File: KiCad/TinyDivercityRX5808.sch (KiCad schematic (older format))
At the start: 18 parts

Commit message: Prototype board is ready
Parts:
- removed J?: RXA, symbol Conn_01x08
- removed J?: RXB, symbol Conn_01x08
- removed J?: Video, symbol Conn_01x02
- removed J?: Googles, symbol Conn_01x05
- removed SW?: SW_Push, symbol SW_Push
- added D2: LED, LEDs:LED_0603, symbol LED
- added J1: Googles, Pin_Headers:Pin_Header_Angled_1x09_Pitch2.54mm, symbol Conn_01x09
- added J2: RX_A, Pin_Headers:Pin_Header_Straight_1x09_Pitch2.54mm, symbol Conn_01x09
- added J3: RX_B, Pin_Headers:Pin_Header_Straight_1x09_Pitch2.54mm, symbol Conn_01x09
- added J4: PROG, Pin_Headers:Pin_Header_Straight_2x05_Pitch2.54mm, symbol Conn_02x05_Odd_Even
- added JP1: Jumper, Pin_Headers:Pin_Header_Straight_1x02_Pitch2.54mm, symbol Jumper
- added R7: 30, Resistors_SMD:R_0603, symbol R
- added R8: 1K, Resistors_SMD:R_0603, symbol R
- added R9: 10K, Resistors_SMD:R_0603, symbol R
- added SW1: SW_DPST, Buttons_Switches_THT:SW_PUSH_6mm_h7.3mm, symbol SW_DPST
- R6: renamed from R?; value 300 -> 1K
- gave numbers to parts that had none: 12
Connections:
- net labels added: AUD_IN, AUD_OUT, MISO, MOSI, RST
- wire segments 67 -> 82
- no-connect marks 0 -> 5
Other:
- moved on the sheet: D1, R4, R5, R6

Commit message: Modified test board
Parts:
- added JP2: JVB, Pin_Headers:Pin_Header_Straight_1x02_Pitch2.54mm, symbol Jumper
- added JP3: JWA, Pin_Headers:Pin_Header_Straight_1x02_Pitch2.54mm, symbol Jumper
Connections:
- net VideoA: now also JP3.1; no longer U1.4 (NC)
- net VideoB: now also JP2.1; no longer U1.6 (NO)
- new net: JP3.2, U1.4 (NC)
- new net: JP2.2, U1.6 (NO)
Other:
- moved on the sheet: JP1
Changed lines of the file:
@@
 $EndComp
 $Comp
-L GND #PWR12
+L GND #PWR11
 U 1 1 5A0C59D1
 P 7000 3700
-F 0 "#PWR12" H 7000 3450 50  0001 C CNN
+F 0 "#PWR11" H 7000 3450 50  0001 C CNN
 F 1 "GND" H 7000 3550 50  0000 C CNN
 F 2 "" H 7000 3700 50  0001 C CNN
@@
 	1    0    0    -1
 $EndComp
-Text Label 6350 2650 2    60   ~ 0
-VideoA
-Text Label 6350 2450 2    60   ~ 0
-VideoB
 Text Label 2800 3950 2    60   ~ 0
 VideoOut
@@
 $EndComp
 $Comp
-L VCC #PWR11
+L VCC #PWR13
 U 1 1 5A0C6148
-P 7000 2250
-F 0 "#PWR11" H 7000 2100 50  0001 C CNN
-F 1 "VCC" H 7000 2400 50  0000 C CNN
-F 2 "" H 7000 2250 50  0001 C CNN
-F 3 "" H 7000 2250 50  0001 C CNN
-	1    7000 2250
+P 7600 2850
+F 0 "#PWR13" H 7600 2700 50  0001 C CNN
+F 1 "VCC" H 7600 3000 50  0000 C CNN
+F 2 "" H 7600 2850 50  0001 C CNN
+F 3 "" H 7600 2850 50  0001 C CNN
+	1    7600 2850
 	1    0    0    -1
 $EndComp
@@
 	3900 2450 5250 2450
 Wire Wire Line
-	5850 2650 6350 2650
-Wire Wire Line
-	5850 2450 6350 2450
-Wire Wire Line
 	5250 2650 4700 2650
 Wire Wire Line
@@
 Connection ~ 7450 4700
 $Comp
-L GND #PWR13
+L GND #PWR12
 U 1 1 5A0DC14E
 P 7450 4850
-F 0 "#PWR13" H 7450 4600 50  0001 C CNN
+F 0 "#PWR12" H 7450 4600 50  0001 C CNN
 F 1 "GND" H 7450 4700 50  0000 C CNN
 F 2 "" H 7450 4850 50  0001 C CNN
@@
 L Jumper JP1
 U 1 1 5A0DEF62
-P 7000 2550
-F 0 "JP1" H 7000 2700 50  0000 C CNN
-F 1 "Jumper" H 7000 2470 50  0000 C CNN
-F 2 "Pin_Headers:Pin_Header_Straight_1x02_Pitch2.54mm" H 7000 2550 50  0001 C CNN
-F 3 "" H 7000 2550 50  0001 C CNN
-	1    7000 2550
-	0    1    1    0
+P 7300 2850
+F 0 "JP1" H 7300 3000 50  0000 C CNN
+F 1 "Jumper" H 7300 2770 50  0000 C CNN
+F 2 "Pin_Headers:Pin_Header_Straight_1x02_Pitch2.54mm" H 7300 2850 50  0001 C CNN
+F 3 "" H 7300 2850 50  0001 C CNN
+	1    7300 2850
+	-1   0    0    1
 $EndComp
 Connection ~ 7000 2850
@@
 RST
 Connection ~ 7600 4000
+$Comp
+L Jumper JP2
+U 1 1 5A25249A
+P 7300 2050
+F 0 "JP2" H 7300 2200 50  0000 C CNN
+F 1 "JVB" H 7300 1970 50  0000 C CNN
+F 2 "Pin_Headers:Pin_Header_Straight_1x02_Pitch2.54mm" H 7300 2050 50  0001 C CNN
+F 3 "" H 7300 2050 50  0001 C CNN
+	1    7300 2050
+	-1   0    0    1
+$EndComp
+$Comp
+L Jumper JP3
+U 1 1 5A252514
+P 7300 2400
+F 0 "JP3" H 7300 2550 50  0000 C CNN
+F 1 "JWA" H 7300 2320 50  0000 C CNN
+F 2 "Pin_Headers:Pin_Header_Straight_1x02_Pitch2.54mm" H 7300 2400 50  0001 C CNN
+F 3 "" H 7300 2400 50  0001 C CNN
+	1    7300 2400
+	-1   0    0    1
+$EndComp
+Wire Wire Line
+	5850 2450 6750 2450
+Wire Wire Line
+	6750 2450 6750 2050
+Wire Wire Line
+	6750 2050 7000 2050
+Wire Wire Line
+	7600 2050 8050 2050
+Text Label 8050 2050 2    60   ~ 0
+VideoB
+Wire Wire Line
+	7600 2400 8050 2400
+Text Label 8050 2400 2    60   ~ 0
+VideoA
+Wire Wire Line
+	5850 2650 6900 2650
+Wire Wire Line
+	6900 2650 6900 2400
+Wire Wire Line
+	6900 2400 7000 2400
 $EndSCHEMATC

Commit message: Second version of prototype board is ready
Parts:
- removed JP2: JVB, Pin_Headers:Pin_Header_Straight_1x02_Pitch2.54mm, symbol Jumper
- removed JP3: JWA, Pin_Headers:Pin_Header_Straight_1x02_Pitch2.54mm, symbol Jumper
- added C5: 100n, Capacitors_SMD:C_0603, symbol C
- added C6: 10n, Capacitors_SMD:C_0603, symbol C
- added D3: D_Schottky, Diodes_SMD:D_SOD-123, symbol D_Schottky
- added JP2: Video4/5, Pin_Headers:Pin_Header_Straight_1x03_Pitch2.54mm, symbol Jumper_NC_Dual
- added U3: MAX4625, TO_SOT_Packages_SMD:SOT-23-6, symbol MAX4624/5
- U1: value MAX4624/5 -> MAX4624
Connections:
- net GND: now also C5.1, C6.1, U3.3 (GND)
- net MOSI: now also U3.1 (IN)
- net RSSI_A: now also JP1.2, U2.2 (PB3(XTAL1/CLKI/~OC1B~/ADC3/PCINT3)); no longer J4.7 (Pin_7), U2.7 (PB2(SCK/USCK/SCL/T0/INT0/ADC1/PCINT2))
- net VCC: now also D3.2 (A); no longer JP1.1
- net VideoA: now also U1.4 (NC), U3.4 (NC)
- net VideoB: now also U1.6 (NO), U3.6 (NO)
- net VideoOut: now also JP2.2; no longer U1.5 (COM)
- net SCK: now reaches R6.1
- net SCK: now also J4.7 (Pin_7), U2.7 (PB2(SCK/USCK/SCL/T0/INT0/ADC1/PCINT2)); no longer U2.2 (PB3(XTAL1/CLKI/~OC1B~/ADC3/PCINT3))
- net PROG_PWR: now reaches C1.1, C2.1, C3.2, C4.2, J4.2 (Pin_2), R9.2, U1.2 (VCC), U2.8 (VCC)
- net PROG_PWR: now also C5.2, C6.2, D3.1 (K), U3.2 (VCC); no longer JP1.2
- net RSSI_G: now reaches J1.6 (Pin_6)
- net RSSI_G: now also JP1.1
- new net: JP2.3, U1.5 (COM)
- new net: JP2.1, U3.5 (COM)
- no-connect marks 5 -> 4

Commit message: First draft of final PCB
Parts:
- removed C5: 100n, Capacitors_SMD:C_0603, symbol C
- removed C6: 10n, Capacitors_SMD:C_0603, symbol C
- removed J4: PROG, Pin_Headers:Pin_Header_Straight_2x05_Pitch2.54mm, symbol Conn_02x05_Odd_Even
- removed JP1: Jumper, Pin_Headers:Pin_Header_Straight_1x02_Pitch2.54mm, symbol Jumper
- removed JP2: Video4/5, Pin_Headers:Pin_Header_Straight_1x03_Pitch2.54mm, symbol Jumper_NC_Dual
- removed SW1: SW_DPST, Buttons_Switches_THT:SW_PUSH_6mm_h7.3mm, symbol SW_DPST
- removed U2: ATTINY85-20SU, Housings_SOIC:SOIC-8_3.9x4.9mm_Pitch1.27mm, symbol ATTINY85-20SU
- removed U3: MAX4625, TO_SOT_Packages_SMD:SOT-23-6, symbol MAX4624/5
- added J4: Conn_01x06, KiCadCustomLibs:Pads_prog_6pin1.25mm, symbol Conn_01x06
- added SW1: SW_Push, KiCadCustomLibs:Button_TS-018, symbol SW_Push
- added U2: ATTINY85-20MU, Housings_DFN_QFN:QFN-20-1EP_4x4mm_Pitch0.5mm, symbol ATTINY85-20MU
- D1, D2: footprint LEDs:LED_0603 -> LEDs:LED_0805
- D3: footprint Diodes_SMD:D_SOD-123 -> Diodes_SMD:D_SOD-523
- J1: footprint Pin_Headers:Pin_Header_Angled_1x09_Pitch2.54mm -> Connectors_Molex:Molex_PicoBlade_53047-0910_09x1.25mm_Straight
- J2, J3: footprint Pin_Headers:Pin_Header_Straight_1x09_Pitch2.54mm -> Connectors_Molex:Molex_PicoBlade_53048-0910_09x1.25mm_Angled
- renumbered R8 to R7, R7 to R8
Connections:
- net RSSI_G is gone; now on net RSSI_A: J1.6 (Pin_6)
- net GND: now also J4.3 (Pin_3), SW1.1, U2.8 (GND)
- net MISO: now also J4.6 (Pin_6), U2.12 (PB1(MISO/DO/AIN1/OC0B/OC1A/PCINT1))
- net MOSI: now also J4.2 (Pin_2), U2.11 (PB0(MOSI/DI/SDA/AIN0/OC0A/OC1A/AREF/PCINT0))
- net PROG_PWR: now also J4.1 (Pin_1), U2.15 (VCC)
- net RSSI_A: now also U2.2 (PB3(XTAL1/CLKI/OC1B/ADC3/PCINT3))
- net RSSI_B: now also U2.5 (PB4(XTAL2/CLKO/OC1B/ADC2/PCINT4))
- net RST: now also J4.4 (Pin_4), SW1.2, U2.1 (PB5(~RESET~/dW/ADC0/PCINT5))
- net SCK: now also J4.5 (Pin_5), U2.14 (PB2(SCK/USCK/SCL/T0/INT0/ADC1/PCINT2))
- net VideoOut: now also U1.5 (COM)
- no-connect marks 4 -> 1

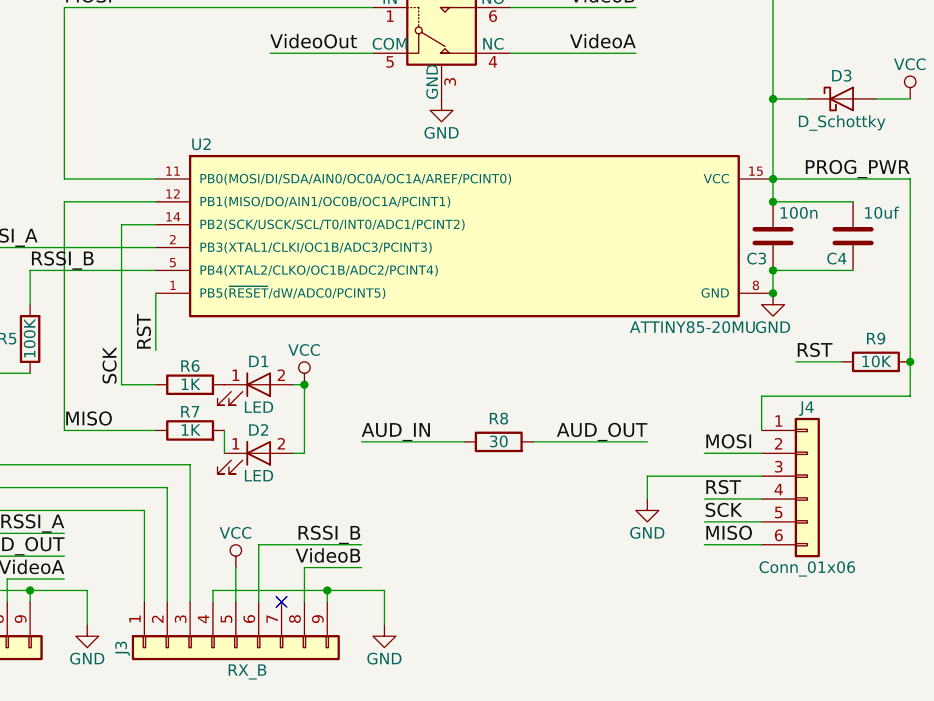
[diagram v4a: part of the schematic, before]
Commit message: Changed attiny case from QFN to SOIC8
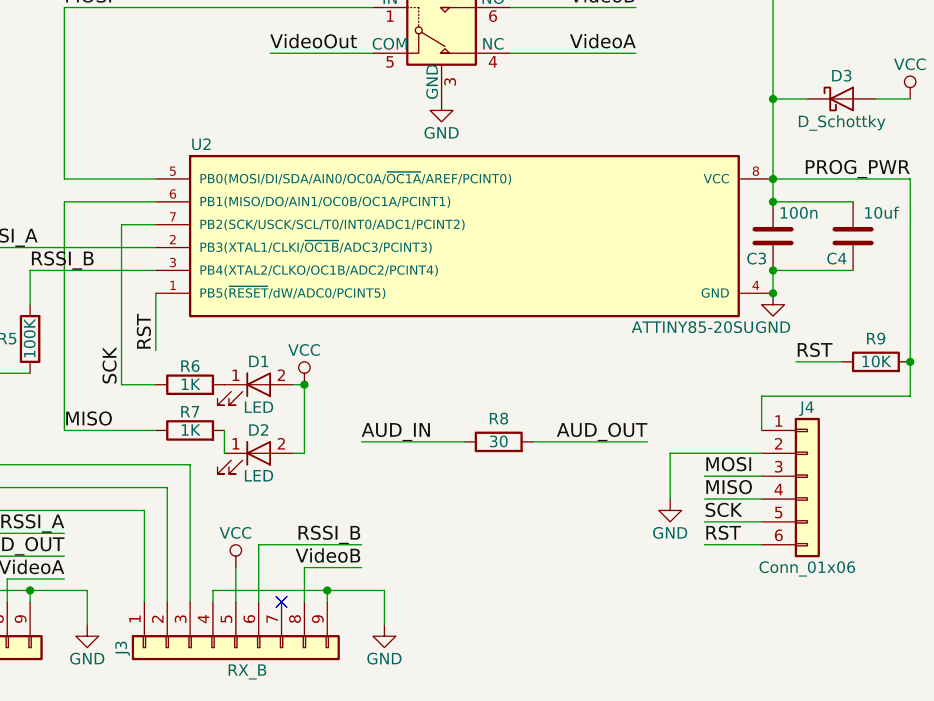
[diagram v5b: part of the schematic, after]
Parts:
- removed U2: ATTINY85-20MU, Housings_DFN_QFN:QFN-20-1EP_4x4mm_Pitch0.5mm, symbol ATTINY85-20MU
- added U2: ATTINY85-20SU, Housings_SOIC:SOIJ-8_5.3x5.3mm_Pitch1.27mm, symbol ATTINY85-20SU
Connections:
- net GND: now also J4.2 (Pin_2), U2.4 (GND); no longer J4.3 (Pin_3)
- net MISO: now also J4.4 (Pin_4), U2.6 (PB1(MISO/DO/AIN1/OC0B/OC1A/PCINT1)); no longer J4.6 (Pin_6)
- net MOSI: now also J4.3 (Pin_3), U2.5 (PB0(MOSI/DI/SDA/AIN0/OC0A/~OC1A~/AREF/PCINT0)); no longer J4.2 (Pin_2)
- net PROG_PWR: now also U2.8 (VCC)
- net RSSI_A: now also U2.2 (PB3(XTAL1/CLKI/~OC1B~/ADC3/PCINT3))
- net RSSI_B: now also U2.3 (PB4(XTAL2/CLKO/OC1B/ADC2/PCINT4))
- net RST: now also J4.6 (Pin_6), U2.1 (PB5(~RESET~/dW/ADC0/PCINT5)); no longer J4.4 (Pin_4)
- net SCK: now also U2.7 (PB2(SCK/USCK/SCL/T0/INT0/ADC1/PCINT2))
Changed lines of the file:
@@
 $EndComp
 $Comp
-L GND #PWR10
+L GND #PWR01
 U 1 1 5A0C59A7
 P 5550 2850
-F 0 "#PWR10" H 5550 2600 50  0001 C CNN
+F 0 "#PWR01" H 5550 2600 50  0001 C CNN
 F 1 "GND" H 5550 2700 50  0000 C CNN
 F 2 "" H 5550 2850 50  0001 C CNN
@@
 $EndComp
 $Comp
-L GND #PWR12
+L GND #PWR02
 U 1 1 5A0C59D1
 P 7000 3700
-F 0 "#PWR12" H 7000 3450 50  0001 C CNN
+F 0 "#PWR02" H 7000 3450 50  0001 C CNN
 F 1 "GND" H 7000 3550 50  0000 C CNN
 F 2 "" H 7000 3700 50  0001 C CNN
@@
 RSSI_B
 $Comp
-L GND #PWR1
+L GND #PWR03
 U 1 1 5A0C5ED9
 P 2550 2800
-F 0 "#PWR1" H 2550 2550 50  0001 C CNN
+F 0 "#PWR03" H 2550 2550 50  0001 C CNN
 F 1 "GND" H 2550 2650 50  0000 C CNN
 F 2 "" H 2550 2800 50  0001 C CNN
@@
 $EndComp
 $Comp
-L VCC #PWR13
+L VCC #PWR04
 U 1 1 5A0C6148
 P 7600 2850
-F 0 "#PWR13" H 7600 2700 50  0001 C CNN
+F 0 "#PWR04" H 7600 2700 50  0001 C CNN
 F 1 "VCC" H 7600 3000 50  0000 C CNN
 F 2 "" H 7600 2850 50  0001 C CNN
@@
 $EndComp
 $Comp
-L VCC #PWR2
+L VCC #PWR05
 U 1 1 5A0C6355
 P 3050 4250
-F 0 "#PWR2" H 3050 4100 50  0001 C CNN
+F 0 "#PWR05" H 3050 4100 50  0001 C CNN
 F 1 "VCC" H 3050 4400 50  0000 C CNN
 F 2 "" H 3050 4250 50  0001 C CNN
@@
 $EndComp
 $Comp
-L GND #PWR8
+L GND #PWR06
 U 1 1 5A0C6978
 P 5000 2200
-F 0 "#PWR8" H 5000 1950 50  0001 C CNN
+F 0 "#PWR06" H 5000 1950 50  0001 C CNN
 F 1 "GND" H 5000 2050 50  0000 C CNN
 F 2 "" H 5000 2200 50  0001 C CNN
@@
 $EndComp
 $Comp
-L VCC #PWR7
+L VCC #PWR07
 U 1 1 5A0C6F3D
 P 4950 4100
-F 0 "#PWR7" H 4950 3950 50  0001 C CNN
+F 0 "#PWR07" H 4950 3950 50  0001 C CNN
 F 1 "VCC" H 4950 4250 50  0000 C CNN
 F 2 "" H 4950 4100 50  0001 C CNN
@@
 $EndComp
 $Comp
-L GND #PWR4
+L GND #PWR08
 U 1 1 5A0C7B39
 P 3500 4050
-F 0 "#PWR4" H 3500 3800 50  0001 C CNN
+F 0 "#PWR08" H 3500 3800 50  0001 C CNN
 F 1 "GND" H 3500 3900 50  0000 C CNN
 F 2 "" H 3500 4050 50  0001 C CNN
@@
 $EndComp
 $Comp
-L GND #PWR5
+L GND #PWR09
 U 1 1 5A0C82E6
 P 4000 5150
-F 0 "#PWR5" H 4000 4900 50  0001 C CNN
+F 0 "#PWR09" H 4000 4900 50  0001 C CNN
 F 1 "GND" H 4000 5000 50  0000 C CNN
 F 2 "" H 4000 5150 50  0001 C CNN
@@
 $EndComp
 $Comp
-L GND #PWR9
+L GND #PWR010
 U 1 1 5A0C83DD
 P 5300 5150
-F 0 "#PWR9" H 5300 4900 50  0001 C CNN
+F 0 "#PWR010" H 5300 4900 50  0001 C CNN
 F 1 "GND" H 5300 5000 50  0000 C CNN
 F 2 "" H 5300 5150 50  0001 C CNN
@@
 $EndComp
 $Comp
-L VCC #PWR3
+L VCC #PWR011
 U 1 1 5A0C85A9
 P 3350 4900
-F 0 "#PWR3" H 3350 4750 50  0001 C CNN
+F 0 "#PWR011" H 3350 4750 50  0001 C CNN
 F 1 "VCC" H 3350 5050 50  0000 C CNN
 F 2 "" H 3350 4900 50  0001 C CNN
@@
 $EndComp
 $Comp
-L VCC #PWR6
+L VCC #PWR012
 U 1 1 5A0C85E1
 P 4650 4900
-F 0 "#PWR6" H 4650 4750 50  0001 C CNN
+F 0 "#PWR012" H 4650 4750 50  0001 C CNN
 F 1 "VCC" H 4650 5050 50  0000 C CNN
 F 2 "" H 4650 4900 50  0001 C CNN
@@
 Text Label 3900 2450 0    60   ~ 0
 MOSI
-Wire Wire Line
-	6950 4400 6700 4400
-Text Label 6700 4400 0    60   ~ 0
+Text Label 6700 4500 0    60   ~ 0
 MOSI
 Wire Wire Line
@@
 Wire Wire Line
 	6950 4600 6700 4600
-Text Label 6700 4600 0    60   ~ 0
+Text Label 6700 4800 0    60   ~ 0
 RST
 Wire Wire Line
@@
 Wire Wire Line
 	6950 4800 6700 4800
-Text Label 6700 4800 0    60   ~ 0
+Text Label 6700 4600 0    60   ~ 0
 MISO
 Wire Wire Line
@@
 	3900 2450 5250 2450
 $Comp
-L ATTINY85-20MU U2
-U 1 1 5A3912D6
-P 5650 3450
-F 0 "U2" H 4500 3850 50  0000 C CNN
-F 1 "ATTINY85-20MU" H 6650 3050 50  0000 C CNN
-F 2 "Housings_DFN_QFN:QFN-20-1EP_4x4mm_Pitch0.5mm" H 6500 3450 50  0001 C CIN
-F 3 "" H 5650 3450 50  0001 C CNN
-	1    5650 3450
-	1    0    0    -1
-$EndComp
-$Comp
 L Conn_01x06 J4
 U 1 1 5A3920B9
@@
 Wire Wire Line
 	6950 4150 6950 4300
-Wire Wire Line
-	6950 4500 6450 4500
-Wire Wire Line
-	6450 4500 6450 4600
-$Comp
-L GND #PWR11
+$Comp
+L GND #PWR013
 U 1 1 5A392520
-P 6450 4600
-F 0 "#PWR11" H 6450 4350 50  0001 C CNN
-F 1 "GND" H 6450 4450 50  0000 C CNN
-F 2 "" H 6450 4600 50  0001 C CNN
-F 3 "" H 6450 4600 50  0001 C CNN
-	1    6450 4600
+P 6550 4600
+F 0 "#PWR013" H 6550 4350 50  0001 C CNN
+F 1 "GND" H 6550 4450 50  0000 C CNN
+F 2 "" H 6550 4600 50  0001 C CNN
+F 3 "" H 6550 4600 50  0001 C CNN
+	1    6550 4600
 	1    0    0    -1
 $EndComp
@@
 	1    0    0    -1
 $EndComp
+$Comp
+L ATTINY85-20SU U2
+U 1 1 5A3A564B
+P 5650 3450
+F 0 "U2" H 4500 3850 50  0000 C CNN
+F 1 "ATTINY85-20SU" H 6650 3050 50  0000 C CNN
+F 2 "Housings_SOIC:SOIJ-8_5.3x5.3mm_Pitch1.27mm" H 6600 3450 50  0001 C CIN
+F 3 "" H 5650 3450 50  0001 C CNN
+	1    5650 3450
+	1    0    0    -1
+$EndComp
+Wire Wire Line
+	6950 4500 6700 4500
+Wire Wire Line
+	6550 4600 6550 4400
+Wire Wire Line
+	6550 4400 6950 4400
 $EndSCHEMATC
